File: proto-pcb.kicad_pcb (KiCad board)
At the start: 2 copper layers, 48 x 100 mm, 624 parts

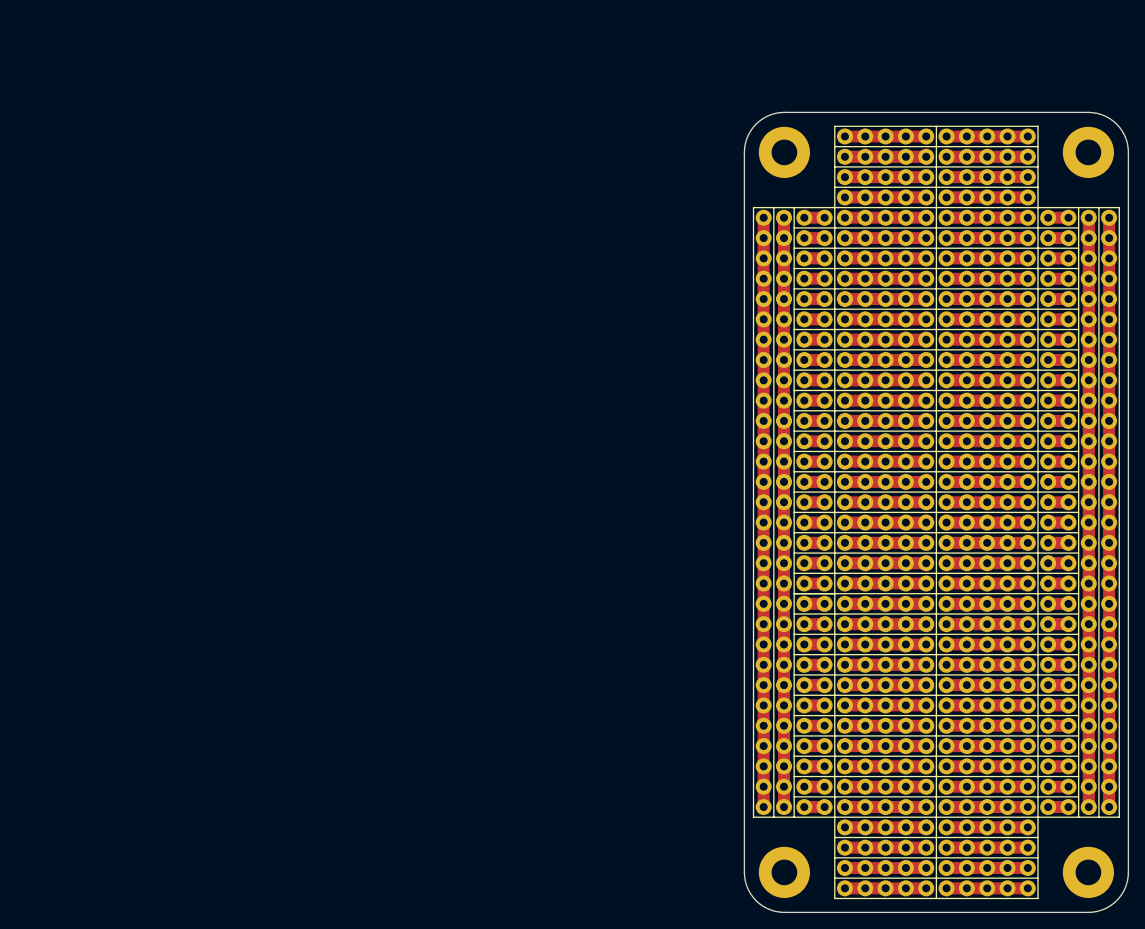
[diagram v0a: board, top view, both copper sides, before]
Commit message: changed mounting hole positions
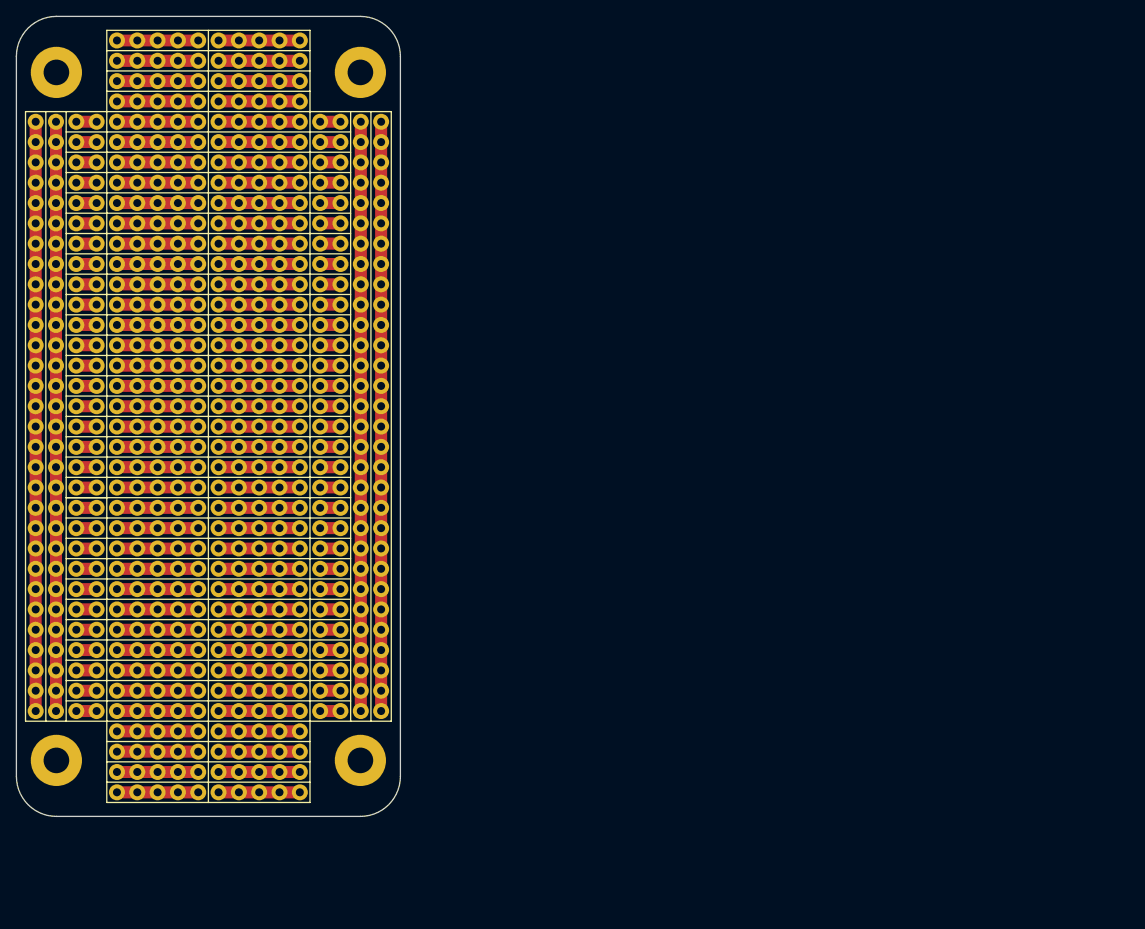
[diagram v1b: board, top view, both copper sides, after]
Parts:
- moved REF** 92.1 mm to (67.7, 130.1)
- moved REF** 92.1 mm to (29.7, 130.1)
- moved REF** 91.8 mm to (65.2, 88.3)
- moved REF** 91.8 mm to (55.0, 90.9)
- moved REF** 91.8 mm to (65.2, 55.3)
- moved REF** 91.8 mm to (65.2, 90.9)
- moved REF** 91.8 mm to (55.0, 131.5)
- moved REF** 91.8 mm to (65.2, 113.7)
- moved REF** 91.8 mm to (55.0, 45.1)
- moved REF** 91.8 mm to (55.0, 103.6)
- moved REF** 91.8 mm to (55.0, 121.3)
- moved REF** 91.8 mm to (55.0, 93.4)
- moved REF** 91.8 mm to (65.2, 83.2)
- moved REF** 91.8 mm to (65.2, 68.0)
- moved REF** 91.8 mm to (55.0, 106.1)
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
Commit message: KiCAD
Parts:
- moved REF** 91.8 mm to (156.2, 100.3)
- moved REF** 91.8 mm to (146.1, 102.9)
- moved REF** 91.8 mm to (156.2, 67.3)
- moved REF** 91.8 mm to (156.2, 102.9)
- moved REF** 91.8 mm to (146.1, 143.5)
- moved REF** 91.8 mm to (156.2, 125.7)
- moved REF** 91.8 mm to (146.1, 57.1)
- moved REF** 91.8 mm to (146.1, 115.6)
- moved REF** 91.8 mm to (146.1, 133.3)
- moved REF** 91.8 mm to (146.1, 105.4)
- moved REF** 91.8 mm to (156.2, 95.2)
- moved REF** 91.8 mm to (156.2, 80.0)
- moved REF** 91.8 mm to (146.1, 118.1)
- moved REF** 91.8 mm to (156.2, 113.0)
- moved REF** 91.8 mm to (146.1, 113.0)
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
